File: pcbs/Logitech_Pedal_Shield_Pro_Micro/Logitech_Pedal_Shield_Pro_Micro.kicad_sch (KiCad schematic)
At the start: 11 parts, among them J1 DB9_Female_MountingHoles, J2 AVR-ISP-6, U1 SparkFun_ProMicro

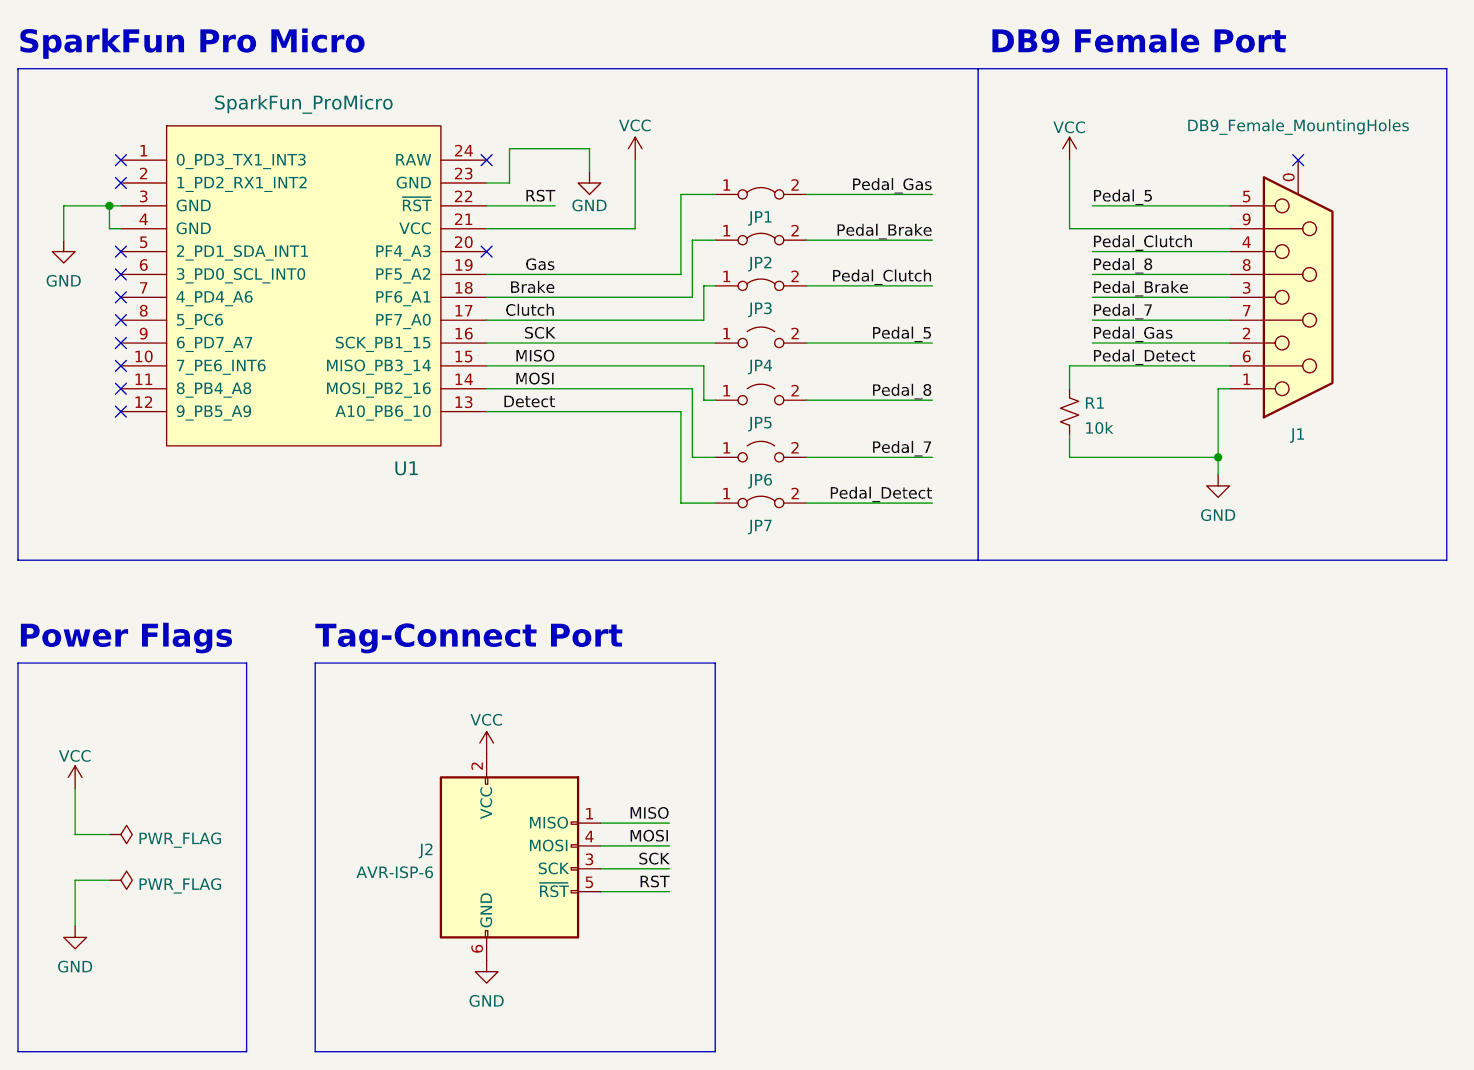
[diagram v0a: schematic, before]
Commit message: Update PCBs to KiCad8 format (8.0.8)
No intended functional changes. Open -> Save -> Close.
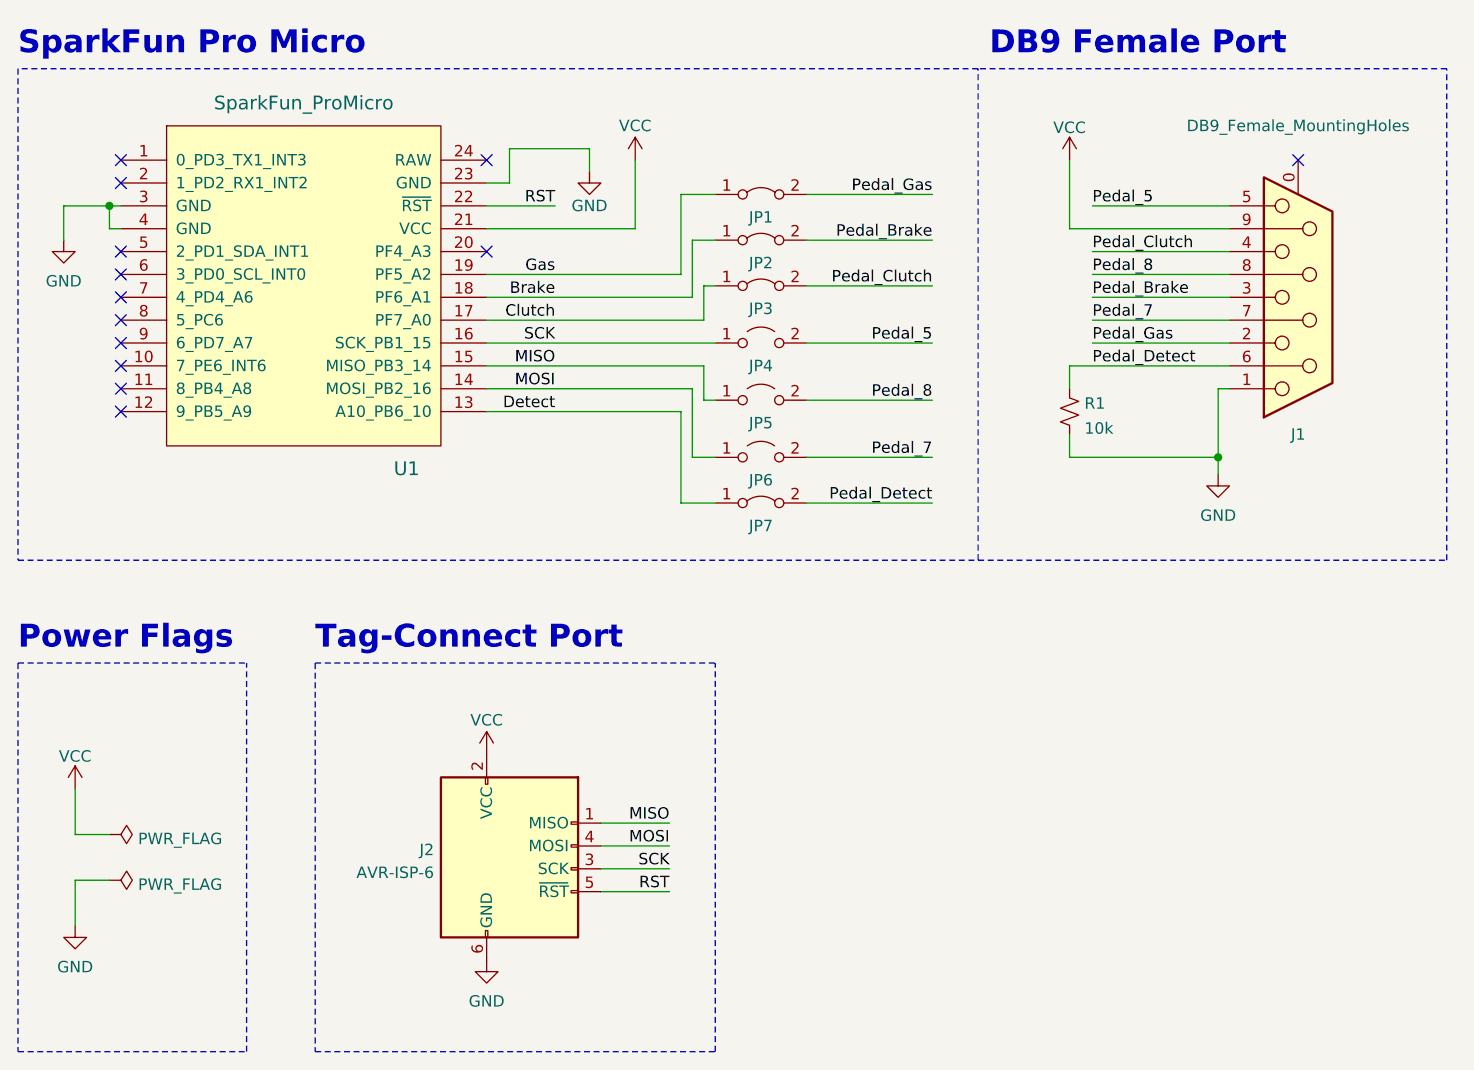
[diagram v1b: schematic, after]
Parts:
- JP1, JP2, JP3, JP7: footprint (none) -> Sim_Racing_Shields:SolderJumper-2_P1.3mm_Bridged_RoundedPad1.0x1.5mm_Unmasked
- U1: footprint (none) -> Sim_Racing_Shields:Sparkfun_ProMicro

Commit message: Relink DE-9 connector symbols (KiCad8)
These symbol names' changed in the included KiCad library.
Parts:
- J1: value DB9_Female_MountingHoles -> DE9_Receptacle_MountingHoles; symbol Connector:DB9_Female_MountingHoles -> Connector:DE9_Receptacle_MountingHoles
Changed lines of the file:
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@@
 	)
 	(symbol
-		(lib_id "Connector:DB9_Female_MountingHoles")
+		(lib_id "Connector:DE9_Receptacle_MountingHoles")
 		(at 196.85 76.2 0)
 		(mirror x)
@@
 			)
 		)
-		(property "Value" "DB9_Female_MountingHoles"
+		(property "Value" "DE9_Receptacle_MountingHoles"
 			(at 196.85 57.15 0)
 			(effects
@@
 			)
 		)
-		(property "Datasheet" " ~"
+		(property "Datasheet" "~"
 			(at 196.85 76.2 0)
 			(effects
@@
 			)
 		)
-		(property "Description" ""
+		(property "Description" "9-pin female receptacle socket D-SUB connector, Mounting Hole"
 			(at 196.85 76.2 0)
 			(effects
